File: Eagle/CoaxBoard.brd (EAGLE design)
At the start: 30.5 x 17.8 mm, 7 parts, among them U1 SN74HC04_INVERTER

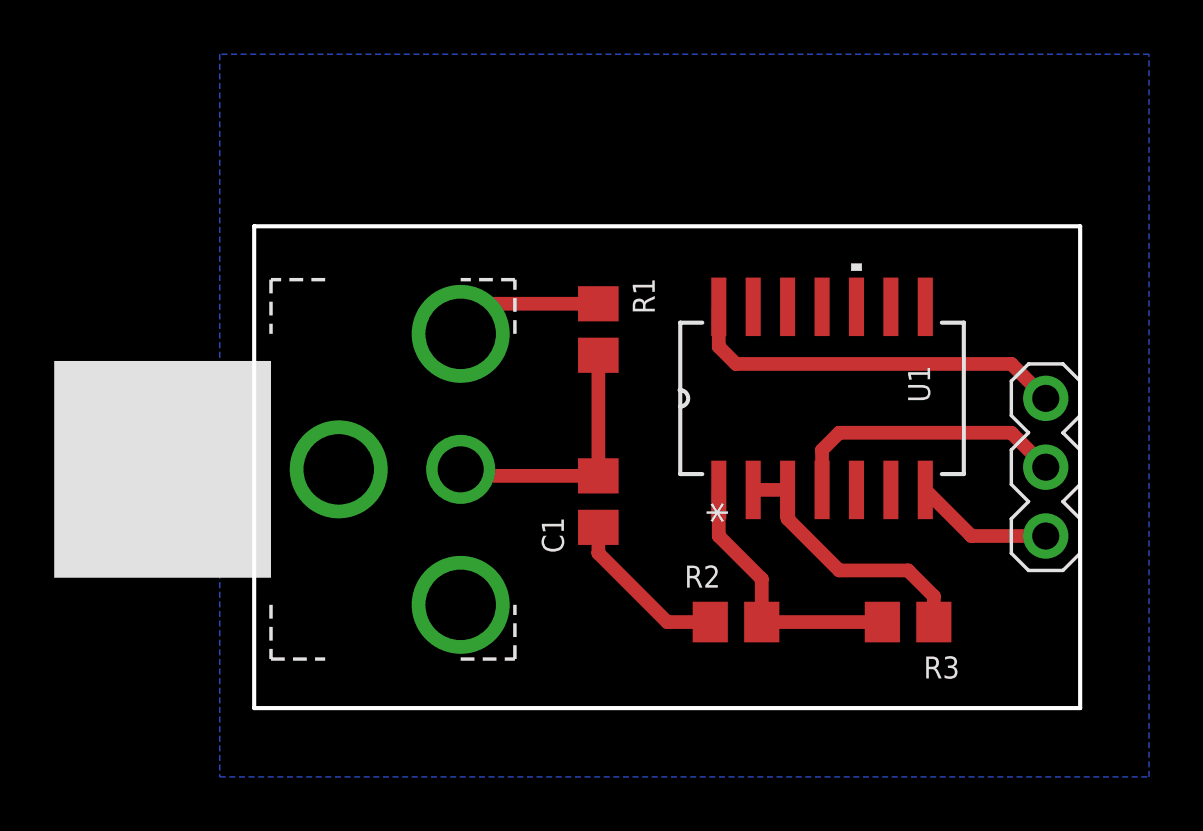
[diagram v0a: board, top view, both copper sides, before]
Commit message: design ordered from Oshpark
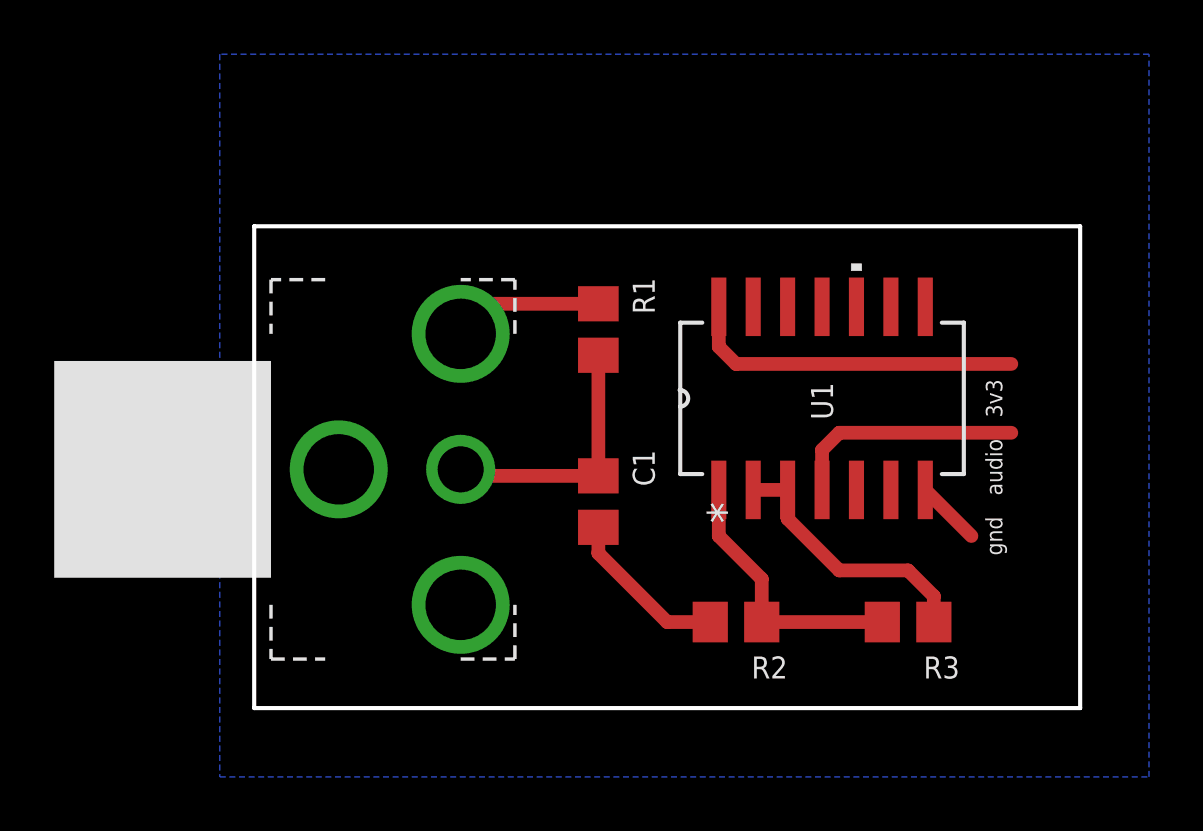
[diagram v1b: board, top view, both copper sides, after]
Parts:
- removed U$2: 1X3HEADER, 1x2HEADER:1X3HEADER
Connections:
- net GND: no longer U$2.P$3
- net SIGNAL: no longer U$2.P$2
- net VCC: no longer U$2.P$1
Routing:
- net GND: track 10.7 -> 7.95 mm
- net VCC: track 14.3 -> 12.5 mm
- net SIGNAL: track 10.5 -> 8.72 mm
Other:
- board text added: "3v3"
- board text added: "S/PDIF-IN COAX"
- board text added: "audio"
- board text added: "gnd"
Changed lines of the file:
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@@
 <layer number="41" name="tRestrict" color="4" fill="10" visible="yes" active="yes"/>
 <layer number="42" name="bRestrict" color="1" fill="10" visible="yes" active="yes"/>
-<layer number="43" name="vRestrict" color="2" fill="10" visible="yes" active="yes"/>
-<layer number="44" name="Drills" color="7" fill="1" visible="no" active="yes"/>
-<layer number="45" name="Holes" color="7" fill="1" visible="no" active="yes"/>
+<layer number="43" name="vRestrict" color="2" fill="10" visible="no" active="yes"/>
+<layer number="44" name="Drills" color="7" fill="1" visible="yes" active="yes"/>
+<layer number="45" name="Holes" color="7" fill="1" visible="yes" active="yes"/>
 <layer number="46" name="Milling" color="3" fill="1" visible="no" active="yes"/>
 <layer number="47" name="Measures" color="7" fill="1" visible="no" active="yes"/>
-<layer number="48" name="Document" color="7" fill="1" visible="yes" active="yes"/>
-<layer number="49" name="Reference" color="7" fill="1" visible="yes" active="yes"/>
+<layer number="48" name="Document" color="7" fill="1" visible="no" active="yes"/>
+<layer number="49" name="Reference" color="7" fill="1" visible="no" active="yes"/>
 <layer number="51" name="tDocu" color="7" fill="1" visible="yes" active="yes"/>
 <layer number="52" name="bDocu" color="7" fill="1" visible="yes" active="yes"/>
@@
 <wire x1="30.48" y1="17.78" x2="30.48" y2="0" width="0.1524" layer="20"/>
 <wire x1="30.48" y1="0" x2="0" y2="0" width="0.1524" layer="20"/>
+<text x="20.32" y="12.7" size="1.4224" layer="26" rot="MR0" align="center">S/PDIF-IN
+COAX</text>
+<text x="27.305" y="11.43" size="0.6096" layer="25" rot="R90" align="center">3v3</text>
+<text x="27.305" y="8.89" size="0.6096" layer="25" rot="R90" align="center">audio</text>
+<text x="27.305" y="6.35" size="0.6096" layer="25" rot="R90" align="center">gnd</text>
 </plain>
 <attributes>
@@
 <elements>
 <element name="C1" library="rcl" library_urn="urn:adsk.eagle:library:334" package="C0805" package3d_urn="urn:adsk.eagle:package:23617/2" value="10n" x="12.7" y="7.62" smashed="yes" rot="R90">
-<attribute name="NAME" x="11.43" y="5.715" size="0.8128" layer="25" rot="R90"/>
+<attribute name="NAME" x="13.97" y="9.525" size="0.8128" layer="25" rot="R270"/>
 <attribute name="POPULARITY" value="88" x="-20.32" y="-20.32" size="1.778" layer="27" rot="R270" display="off"/>
 <attribute name="SPICEPREFIX" value="C" x="-20.32" y="-20.32" size="1.778" layer="27" rot="R270" display="off"/>
@@
 </element>
 <element name="R2" library="resistor" library_urn="urn:adsk.eagle:library:348" package="R0805" package3d_urn="urn:adsk.eagle:package:26059/1" value="100" x="17.78" y="3.175" smashed="yes">
-<attribute name="NAME" x="15.875" y="4.445" size="0.8128" layer="25"/>
+<attribute name="NAME" x="19.685" y="1.905" size="0.8128" layer="25" rot="R180"/>
 </element>
 <element name="R3" library="resistor" library_urn="urn:adsk.eagle:library:348" package="R0805" package3d_urn="urn:adsk.eagle:package:26059/1" value="8k2" x="24.13" y="3.175" smashed="yes">
@@
 </element>
 <element name="U$1" library="COAX_SPDIF" package="RCA_JACK" value="RCA_JACK" x="7.62" y="3.81" smashed="yes" rot="R90"/>
-<element name="U$2" library="1x2HEADER" package="1X3HEADER" value="1X3HEADER" x="27.94" y="12.7" smashed="yes" rot="R270"/>
 <element name="U1" library="COAX_SPDIF" package="NS14" value="SN74HC04_INVERTER" x="20.955" y="11.43" smashed="yes" rot="R90">
 <attribute name="DATASHEET_URL" value="http://www.ti.com/lit/gpn/SN74HC04" x="43.815" y="33.02" size="1.778" layer="27" rot="R90" display="off"/>
@@
 <attribute name="INDUSTRY_STD_PKG_TYPE" value="SO" x="43.815" y="33.02" size="1.778" layer="27" rot="R90" display="off"/>
 <attribute name="MANUFACTURER" value="Texas Instruments" x="43.815" y="33.02" size="1.778" layer="27" rot="R90" display="off"/>
-<attribute name="NAME" x="24.13" y="11.9634" size="0.8128" layer="25" ratio="6" rot="SR90" align="top-center"/>
+<attribute name="NAME" x="20.955" y="11.3284" size="0.8128" layer="25" ratio="6" rot="SR90" align="center"/>
 <attribute name="PACKAGE_DESIGNATOR" value="NS" x="43.815" y="33.02" size="1.778" layer="27" rot="R90" display="off"/>
 <attribute name="PIN_COUNT" value="14" x="43.815" y="33.02" size="1.778" layer="27" rot="R90" display="off"/>
@@
 <contactref element="R1" pad="2"/>
 <contactref element="U1" pad="7"/>
-<contactref element="U$2" pad="P$3"/>
 <polygon width="0.1524" layer="16">
 <vertex x="-1.27" y="24.13"/>
@@
 <wire x1="8.73" y1="14.92" x2="12.7" y2="14.92" width="0.508" layer="1"/>
 <wire x1="24.765" y1="8.0518" x2="26.4668" y2="6.35" width="0.508" layer="1"/>
-<wire x1="26.4668" y1="6.35" x2="29.21" y2="6.35" width="0.508" layer="1"/>
+<wire x1="12.7" y1="14.92" x2="24.765" y2="8.0518" width="0" layer="19" extent="1-1"/>
 </signal>
 <signal name="N$1">
@@
 <signal name="VCC">
 <contactref element="U1" pad="14"/>
-<contactref element="U$2" pad="P$1"/>
 <wire x1="17.145" y1="14.8082" x2="17.145" y2="13.335" width="0.508" layer="1"/>
 <wire x1="17.145" y1="13.335" x2="17.78" y2="12.7" width="0.508" layer="1"/>
-<wire x1="27.94" y1="12.7" x2="29.21" y2="11.43" width="0.508" layer="1"/>
 <wire x1="17.78" y1="12.7" x2="27.94" y2="12.7" width="0.508" layer="1"/>
 </signal>
@@
 </signal>
 <signal name="SIGNAL">
-<contactref element="U$2" pad="P$2"/>
 <contactref element="U1" pad="4"/>
 <wire x1="20.955" y1="8.0518" x2="20.955" y2="9.525" width="0.508" layer="1"/>
 <wire x1="20.955" y1="9.525" x2="21.59" y2="10.16" width="0.508" layer="1"/>
 <wire x1="21.59" y1="10.16" x2="27.94" y2="10.16" width="0.508" layer="1"/>
-<wire x1="27.94" y1="10.16" x2="29.21" y2="8.89" width="0.508" layer="1"/>
+</signal>
+<signal name="N$5">
 </signal>
 </signals>
@@
 </drawing>
 <compatibility>
+<note version="6.3" minversion="6.2.2" severity="warning">
+Since Version 6.2.2 text objects can contain more than one line,
+which will not be processed correctly with this version.
+</note>
 <note version="8.2" severity="warning">
 Since Version 8.2, EAGLE supports online libraries. The ids
